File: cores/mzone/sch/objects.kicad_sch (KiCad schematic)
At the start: 35 parts

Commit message: mzone core
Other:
- note added: "V or VF??"

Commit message: mzone core
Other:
- note removed: "V or VF??"

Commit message: mzone core
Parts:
- added unit 5 of D4
- added unit 3 of D7
- added unit 4 of DE19
- added unit 5 of G5
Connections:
- net PAL3' is gone; now on net PAL'3: D6.19 (Q7)
- net GND: now also D4.7 (GND), D7.7 (GND), DE19.7 (GND), G5.7 (GND)
- net VCC: now also D4.14 (VCC), D7.14 (VCC), DE19.14 (VCC), G5.14 (VCC)
- no-connect marks 8 -> 9

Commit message: mzone core
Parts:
- added unit 2 of D1
- added unit 2 of D3
- added unit 2 of E1
- added unit 2 of E3
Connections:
- net GND: now also D1.14 (GND), D3.14 (GND), E1.14 (GND), E3.14 (GND); no longer D1.14 (GND), D3.14 (GND), E1.14 (GND), E3.14 (GND)
- net VCC: now also D1.1 (VPP), D1.27 (~{PGM}), D1.28 (VCC), D3.1 (VPP), D3.27 (~{PGM}), D3.28 (VCC), E1.1 (VPP), E1.27 (~{PGM}), E1.28 (VCC), E3.1 (VPP), E3.27 (~{PGM}), E3.28 (VCC); no longer D1.1 (VPP), D1.26 (NC), D1.27 (~{PGM}), D1.28 (VCC), D3.1 (VPP), D3.26 (NC), D3.27 (~{PGM}), D3.28 (VCC), E1.1 (VPP), E1.26 (NC), E1.27 (~{PGM}), E1.28 (VCC), E3.1 (VPP), E3.26 (NC), E3.27 (~{PGM}), E3.28 (VCC)
- no-connect marks 9 -> 13

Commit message: mzone core
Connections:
- net VCC: no longer E12.20 (VCC)
- net VSS: no longer E12.10 (VSS)

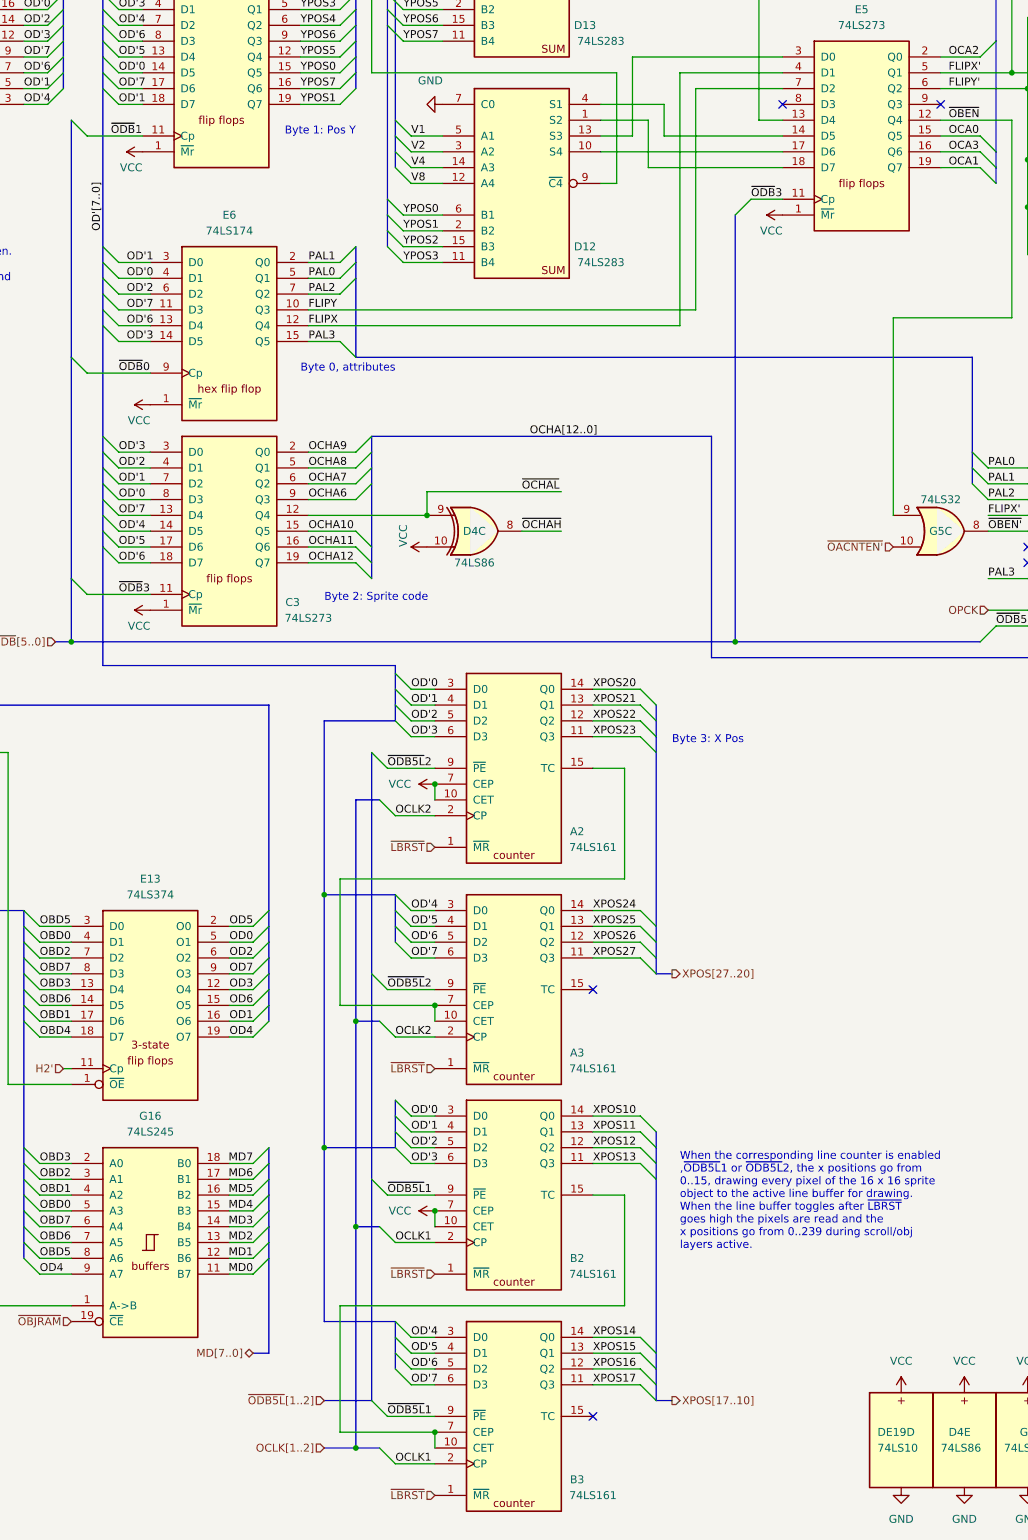
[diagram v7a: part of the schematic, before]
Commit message: mzone core
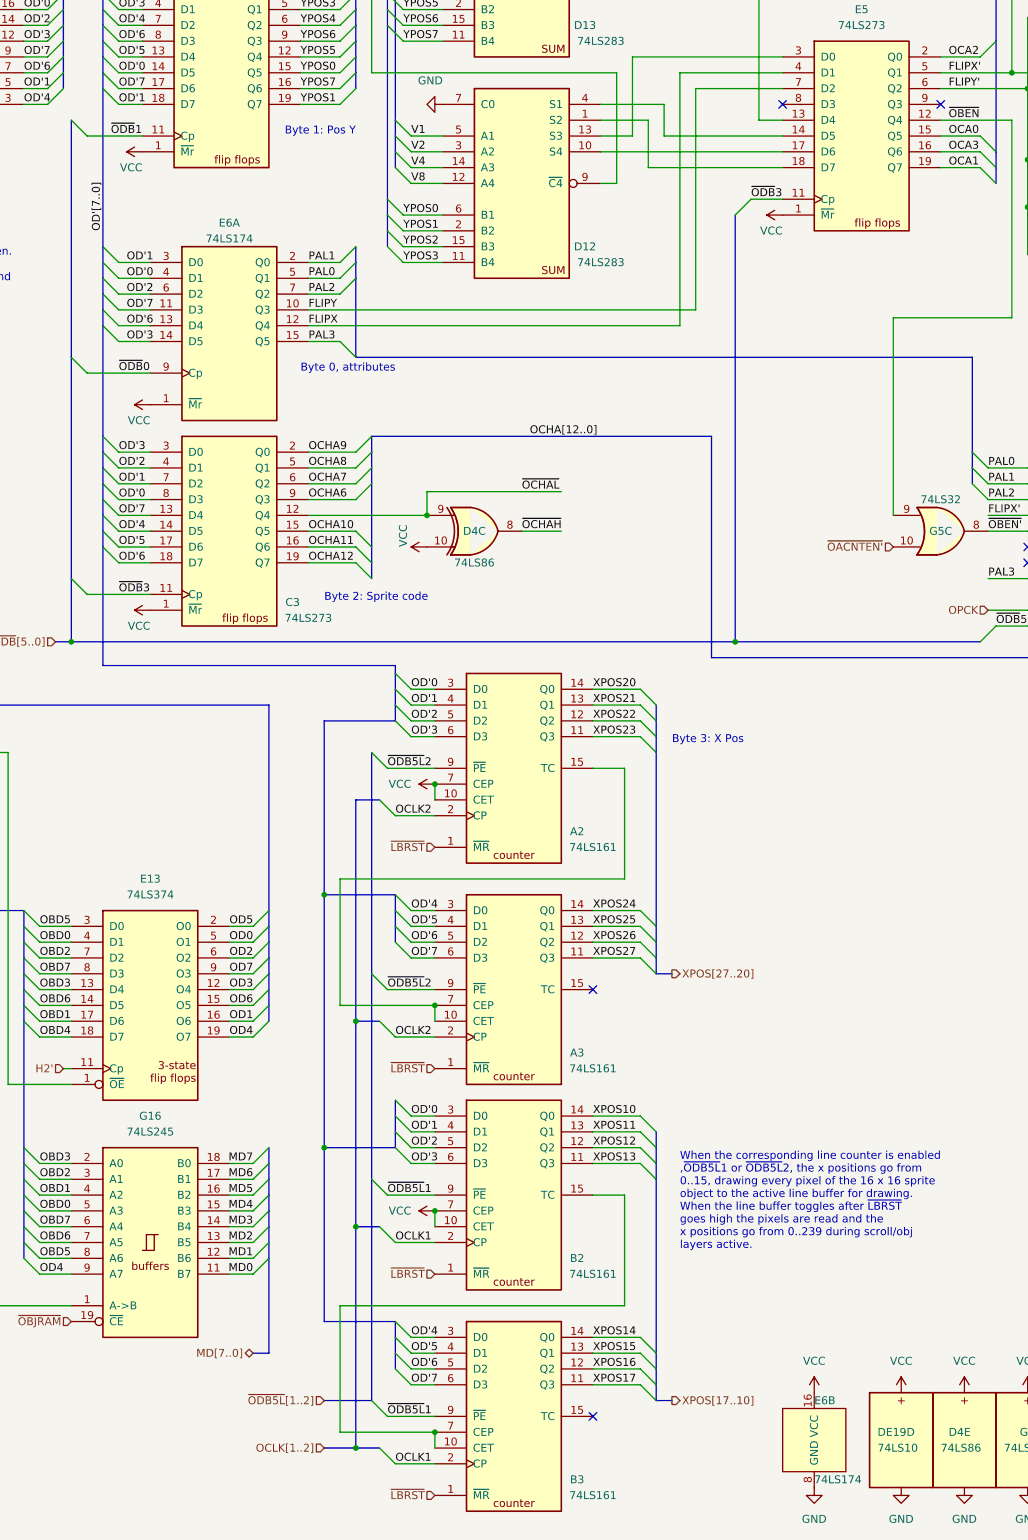
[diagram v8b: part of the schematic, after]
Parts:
- added unit 2 of E6
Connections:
- net GND: now also C3.10 (GND), D11.10 (GND), E5.10 (GND), E6.8 (GND)
- net VCC: now also C3.20 (VCC), D11.20 (VCC), E5.20 (VCC), E6.16 (VCC); no longer E6.16 (VCC)
- removed net VSS: E6.8 (VSS)
